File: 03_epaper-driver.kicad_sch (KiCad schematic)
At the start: 0 parts

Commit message: Add EPD Driver Circuit
Signed-off-by: Anna-Lena Marx <anna-lena.marx@web.de>
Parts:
- added C10, C11, C4, C5, C6, C7, C8, C9: 1uF, Capacitor_SMD:C_1206_3216Metric_Pad1.33x1.80mm_HandSolder, symbol Device:C
- added C2, C3: 4.7uF, Capacitor_SMD:C_1206_3216Metric_Pad1.33x1.80mm_HandSolder, symbol Device:C
- added D1, D2, D3: MBR0530, Diode_SMD:D_SOD-123, symbol Diode:MBR0530
- added J4: Conn_01x24_MountingPin, Connector_FFC-FPC:Hirose_FH12-24S-0.5SH_1x24-1MP_P0.50mm_Horizontal, symbol Connector_Generic_MountingPin:Conn_01x24_MountingPin
- added L1: 10uH 1A, Inductor_SMD:L_1206_3216Metric_Pad1.42x1.75mm_HandSolder, symbol Device:L_Iron
- added Q1: Si1308EDL, Package_TO_SOT_SMD:SOT-323_SC-70, symbol Transistor_FET:Si1308EDL
- added R10: 3, Resistor_SMD:R_1206_3216Metric_Pad1.30x1.75mm_HandSolder, symbol Device:R
- added R8: 10k, Resistor_SMD:R_1206_3216Metric_Pad1.30x1.75mm_HandSolder, symbol Device:R
- added R9: 0.47, Resistor_SMD:R_1206_3216Metric_Pad1.30x1.75mm_HandSolder, symbol Device:R
- added S1: 450404015514, 4504040015514:450404015514, symbol 450404015514:450404015514
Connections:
- new net: C6.2, J4.18 (Pin_18)
- new net: C3.1, D3.2 (A), L1.2, Q1.3 (D)
- new net: C3.2, D1.2 (A), D2.1 (K)
- new net: R9.2, S1.1
- new net: R10.1, S1.3
- new net: C11.2, J4.24 (Pin_24)
- new net: C4.2, J4.5 (Pin_5)
- new net: C9.2, J4.22 (Pin_22)
- new net: C7.2, J4.20 (Pin_20)
- new net +3.3V: C2.1, C5.2, J4.15 (Pin_15), J4.16 (Pin_16), L1.1
- new net EPD_BUSY: J4.9 (Pin_9)
- new net EPD_CS: J4.12 (Pin_12)
- new net EPD_DC: J4.11 (Pin_11)
- new net EPD_DIN: J4.14 (Pin_14)
- new net EPD_RST: J4.10 (Pin_10)
- new net EPD_SCK: J4.13 (Pin_13)
- new net GDR: J4.2 (Pin_2), Q1.1 (G), R8.1
- new net GND: C10.1, C11.1, C2.2, C4.1, C5.1, C6.1, C7.1, C8.1, C9.1, D1.1 (K), J4.17 (Pin_17), J4.8 (Pin_8), J4.MP (MountPin), R10.2, R8.2, R9.1
- new net RESE: J4.3 (Pin_3), Q1.2 (S), S1.2
- new net VGH: C8.2, D3.1 (K), J4.21 (Pin_21)
- new net VGL: C10.2, D2.2 (A), J4.23 (Pin_23)
- no-connect marks 0 -> 5

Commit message: Added some more notes, testpoints and rechecked footprints and parts
Signed-off-by: Anna-Lena Marx <anna-lena.marx@web.de>
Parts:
- removed L1: 10uH 1A, Inductor_SMD:L_1206_3216Metric_Pad1.42x1.75mm_HandSolder, symbol Device:L_Iron
- added L1: 10uH, footprints:IND_IFSC_1515AH_VIS-L, symbol Device:L
- added TP1: EPD_BUSY, TestPoint:TestPoint_Plated_Hole_D2.0mm, symbol Connector:TestPoint
- added TP2: EPD_RST, TestPoint:TestPoint_Plated_Hole_D2.0mm, symbol Connector:TestPoint
- added TP3: EPD_DC, TestPoint:TestPoint_Plated_Hole_D2.0mm, symbol Connector:TestPoint
- added TP4: EPD_CS, TestPoint:TestPoint_Plated_Hole_D2.0mm, symbol Connector:TestPoint
- added TP5: EPD_SCK, TestPoint:TestPoint_Plated_Hole_D2.0mm, symbol Connector:TestPoint
- added TP6: EPD_DIN, TestPoint:TestPoint_Plated_Hole_D2.0mm, symbol Connector:TestPoint
- added TP7: GND, TestPoint:TestPoint_Plated_Hole_D2.0mm, symbol Connector:TestPoint
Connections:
- net +3.3V: now also L1.1
- net EPD_BUSY: now also TP1.1
- net EPD_CS: now also TP4.1
- net EPD_DC: now also TP3.1
- net EPD_DIN: now also TP6.1
- net EPD_RST: now also TP2.1
- net EPD_SCK: now also TP5.1
- net GND: now also TP7.1
- net at C3.1, D3.2 (A), Q1.3 (D): now also L1.2

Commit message: Changed buttons to smaller ones, updated some comments
Signed-off-by: Anna-Lena Marx <anna-lena.marx@web.de>
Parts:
- renumbered TP1 to TP1_EPD_BUSY1, TP2 to TP2_EPD_RST1, TP3 to TP3_EPD_DC1, TP4 to TP4_EPD_CS1, TP5 to TP5_EPD_SCK1, TP6 to TP6_EPD_DIN1, TP7 to TP7_GND1
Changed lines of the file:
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@@
 		(dnp no)
 		(fields_autoplaced yes)
-		(property "Reference" "TP6"
+		(property "Reference" "TP6_EPD_DIN1"
 			(at 77.47 175.2599 90)
 			(effects
@@
 			(project "ZEReader-Pico"
 				(path "/ec954637-2a8b-4662-b4a1-f88107f11cb0/d006ff72-e176-4e99-8906-01d59b86077c"
-					(reference "TP6")
+					(reference "TP6_EPD_DIN1")
 					(unit 1)
 				)
@@
 		(dnp no)
 		(fields_autoplaced yes)
-		(property "Reference" "TP4"
+		(property "Reference" "TP4_EPD_CS1"
 			(at 77.47 165.0999 90)
 			(effects
@@
 			(project "ZEReader-Pico"
 				(path "/ec954637-2a8b-4662-b4a1-f88107f11cb0/d006ff72-e176-4e99-8906-01d59b86077c"
-					(reference "TP4")
+					(reference "TP4_EPD_CS1")
 					(unit 1)
 				)
@@
 		(dnp no)
 		(fields_autoplaced yes)
-		(property "Reference" "TP3"
+		(property "Reference" "TP3_EPD_DC1"
 			(at 77.47 160.0199 90)
 			(effects
@@
 			(project "ZEReader-Pico"
 				(path "/ec954637-2a8b-4662-b4a1-f88107f11cb0/d006ff72-e176-4e99-8906-01d59b86077c"
-					(reference "TP3")
+					(reference "TP3_EPD_DC1")
 					(unit 1)
 				)
@@
 		(dnp no)
 		(fields_autoplaced yes)
-		(property "Reference" "TP7"
+		(property "Reference" "TP7_GND1"
 			(at 77.47 180.3399 90)
 			(effects
@@
 			(project "ZEReader-Pico"
 				(path "/ec954637-2a8b-4662-b4a1-f88107f11cb0/d006ff72-e176-4e99-8906-01d59b86077c"
-					(reference "TP7")
+					(reference "TP7_GND1")
 					(unit 1)
 				)
@@
 		(dnp no)
 		(fields_autoplaced yes)
-		(property "Reference" "TP2"
+		(property "Reference" "TP2_EPD_RST1"
 			(at 77.47 154.9399 90)
 			(effects
@@
 			(project "ZEReader-Pico"
 				(path "/ec954637-2a8b-4662-b4a1-f88107f11cb0/d006ff72-e176-4e99-8906-01d59b86077c"
-					(reference "TP2")
+					(reference "TP2_EPD_RST1")
 					(unit 1)
 				)
@@
 		(dnp no)
 		(fields_autoplaced yes)
-		(property "Reference" "TP1"
+		(property "Reference" "TP1_EPD_BUSY1"
 			(at 77.47 149.8599 90)
 			(effects
@@
 			(project ""
 				(path "/ec954637-2a8b-4662-b4a1-f88107f11cb0/d006ff72-e176-4e99-8906-01d59b86077c"
-					(reference "TP1")
+					(reference "TP1_EPD_BUSY1")
 					(unit 1)
 				)
@@
 		(dnp no)
 		(fields_autoplaced yes)
-		(property "Reference" "TP5"
+		(property "Reference" "TP5_EPD_SCK1"
 			(at 77.47 170.1799 90)
 			(effects
@@
 			(project "ZEReader-Pico"
 				(path "/ec954637-2a8b-4662-b4a1-f88107f11cb0/d006ff72-e176-4e99-8906-01d59b86077c"
-					(reference "TP5")
-					(unit 1)
-				)
+					(reference "TP5_EPD_SCK1")
+					(unit 1)
+				)

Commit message: Added CC line pulldown resistors
Signed-off-by: Anna-Lena Marx <anna-lena.marx@web.de>
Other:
- note added: "Charge pump"
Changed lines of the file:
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@@
 		)
 	)
-	(text_box "Question:\nCan the capacitor value be changed?\nE.g. 10uF to keep the BOM small?\n\n\nUC8179 Datasheet: \n\nNote:\n1. The capacitor value of VGH/VGL must be equal or more than the one of VDH/VDL/VDHR.\n-> can atleast these values be changed to 10uF for all of them? "
+	(text_box "Question:\nCan the capacitor value be changed?\nE.g. 10uF to keep the BOM small? Does this result in negative inrush effects?\n\n\nUC8179 Datasheet: \n\nNote:\n1. The capacitor value of VGH/VGL must be equal or more than the one of VDH/VDL/VDHR.\n-> can atleast these values be changed to 10uF for all of them? \n\nhttps://www.signalintegrityjournal.com/articles/1589-the-myth-of-three-capacitor-values\nhttps://codeinsecurity.wordpress.com/2025/01/25/proper-decoupling-practices-and-why-you-should-leave-100nf-behind/"
 		(exclude_from_sim no)
 		(at 172.72 15.24 0)
-		(size 68.58 25.4)
+		(size 99.06 30.48)
 		(stroke
 			(width 0)
@@
 		)
 	)
+	(text "Charge pump"
+		(exclude_from_sim no)
+		(at 82.804 60.706 0)
+		(effects
+			(font
+				(size 1.27 1.27)
+			)
+		)
+	)

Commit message: fix selfcontainment issues, added 2D rendering
Signed-off-by: Anna-Lena Marx <anna-lena.marx@web.de>
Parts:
- L1: footprint footprints:IND_IFSC_1515AH_VIS-L -> prj-footprints:IND_IFSC_1515AH_VIS-L
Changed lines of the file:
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@@
 			)
 		)
-		(property "Footprint" "footprints:IND_IFSC_1515AH_VIS-L"
+		(property "Footprint" "prj-footprints:IND_IFSC_1515AH_VIS-L"
 			(at 63.5 76.2 0)
 			(effects

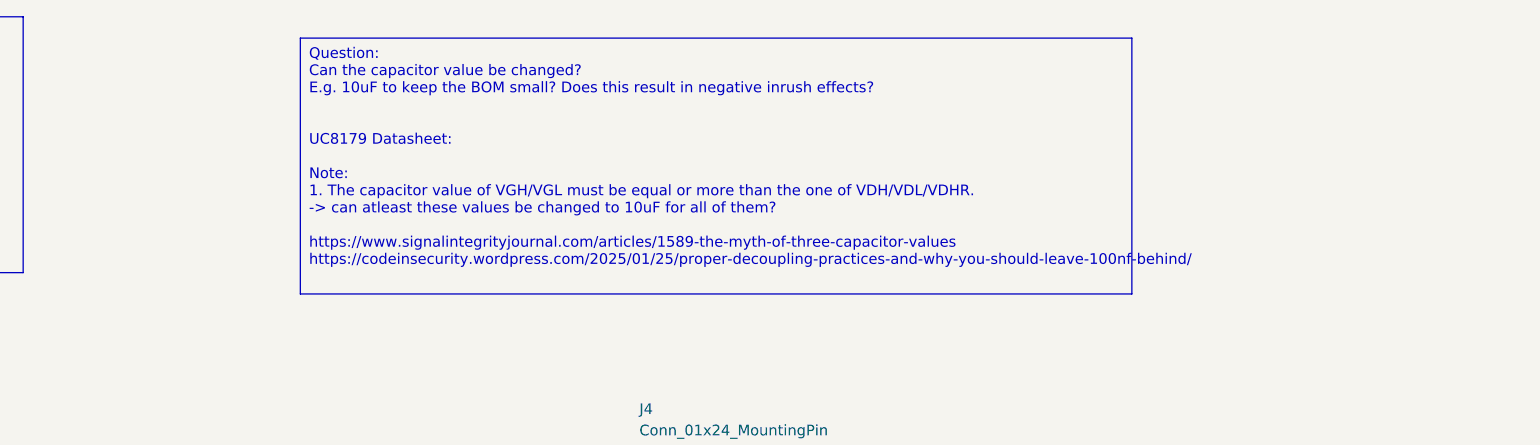
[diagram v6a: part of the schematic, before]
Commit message: selfcontainment, smaller fixes
Signed-off-by: Anna-Lena Marx <anna-lena.marx@web.de>
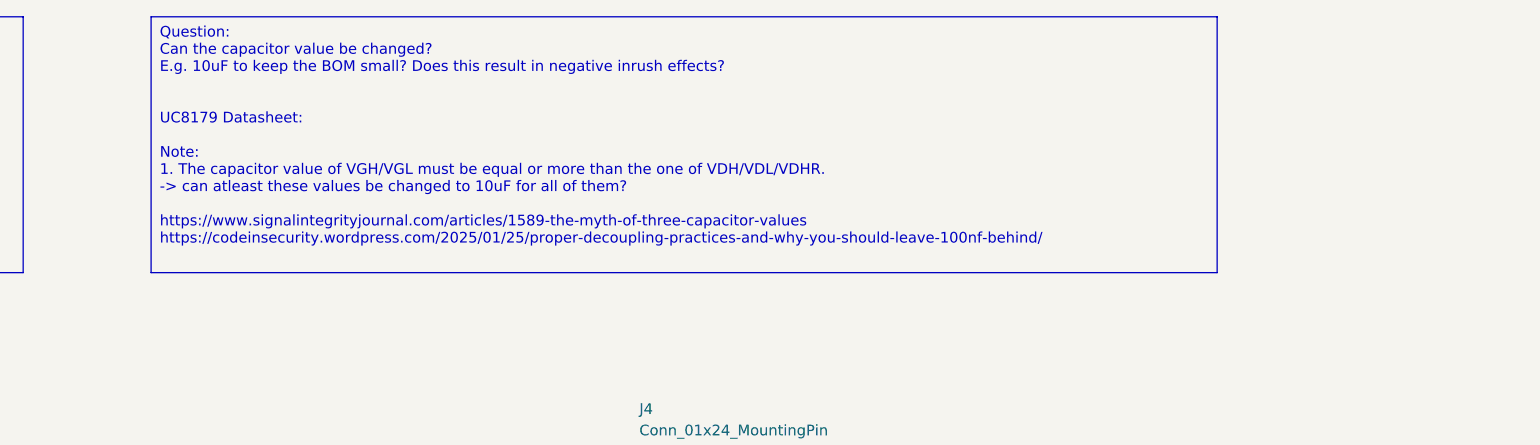
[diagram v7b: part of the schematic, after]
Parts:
- S1: footprint 4504040015514:450404015514 -> prj-footprints:450404015514

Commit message: selfcontainment fixes
Signed-off-by: Anna-Lena Marx <anna-lena.marx@web.de>
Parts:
- S1: Description_1 Slide Switch SPDT Surface Mount -> Slide Switch SPDT Surface Mount
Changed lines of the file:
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@@
 			)
 		)
-		(property "Datasheet" "~"
+		(property "Datasheet" "https://www.vishay.com/docs/34295/ifsc-1515ah-01.pdf"
 			(at 63.5 76.2 0)
 			(effects
@@
 			)
 		)
-		(property "Datasheet" ""
+		(property "Datasheet" "https://www.we-online.com/components/products/datasheet/450404015514.pdf"
 			(at 76.2 124.46 0)
 			(effects
@@
 			)
 		)
-		(property "Description_1" "\n                        \n                            Slide Switch SPDT Surface Mount\n                        \n"
+		(property "Description_1" "Slide Switch SPDT Surface Mount"
 			(at 76.2 124.46 0)
 			(effects
@@
 			)
 		)
-		(property "Datasheet" "~"
+		(property "Datasheet" "https://www.hirose.com/product/document?clcode=&productname=&series=FH12&documenttype=Catalog&lang=en&documentid=D31648_en"
 			(at 215.9 95.25 0)
 			(effects
